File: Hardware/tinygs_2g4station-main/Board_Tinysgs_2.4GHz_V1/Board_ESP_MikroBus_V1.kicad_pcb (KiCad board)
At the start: 2 copper layers, 103.6 x 61.7 mm, 26 parts, among them U1 ESP32-DEVKITC-32D

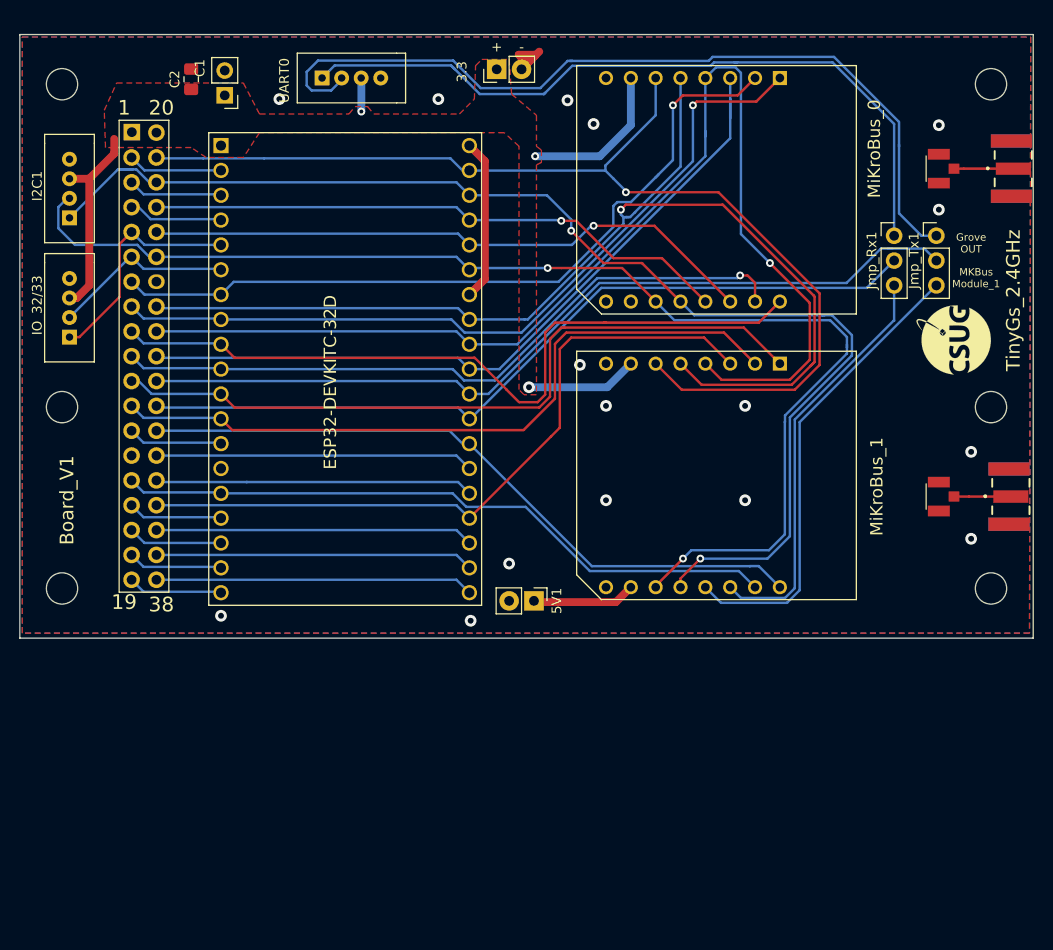
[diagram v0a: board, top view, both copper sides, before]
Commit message: Here is a version with the ISA connector standard. The schematic is ready, but the layout needs to be fixed
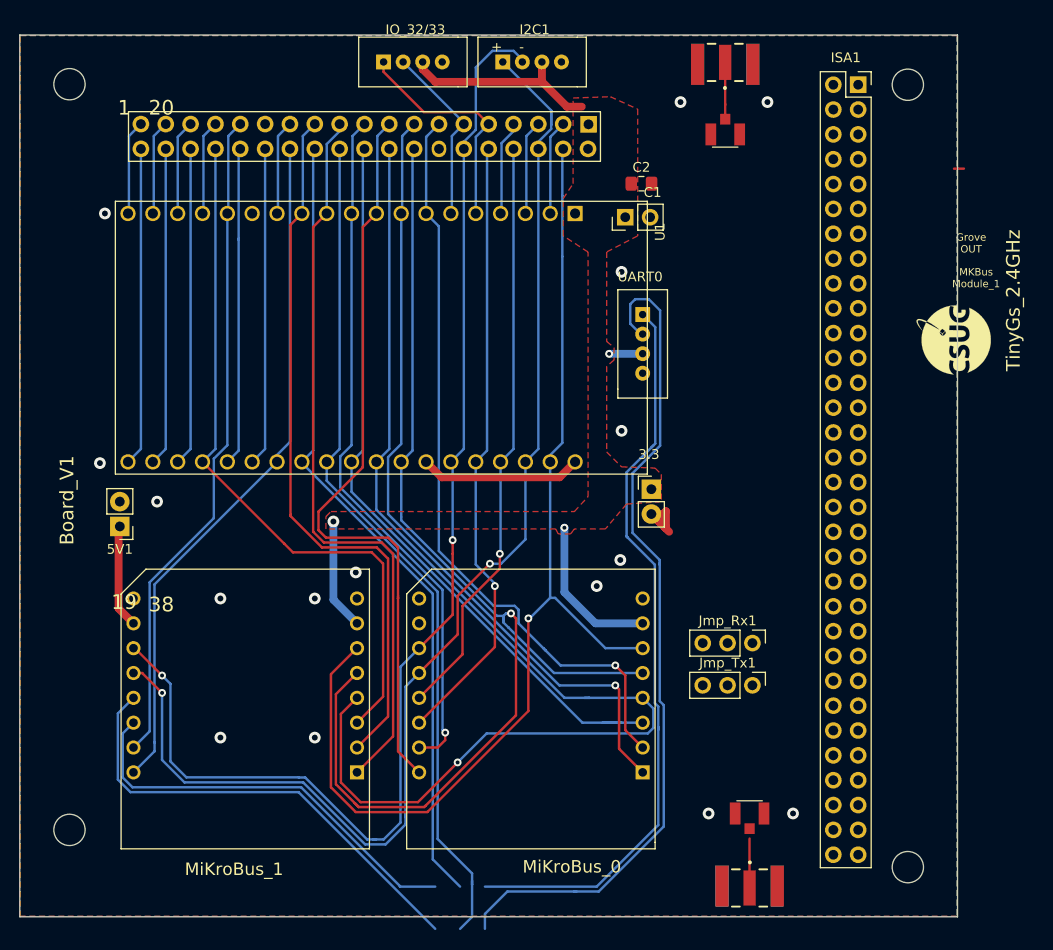
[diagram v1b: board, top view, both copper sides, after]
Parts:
- removed the REF** at (48.0, 55.1)
- removed the REF** at (143.0, 55.1)
- added ISA1: Conn_02x32_Odd_Even, Connector_PinSocket_2.54mm:PinSocket_2x32_P2.54mm_Vertical, F.Cu at (129.4, 22.1)
- U1: footprint ESP32-DEVKITC-32D:MODULE_ESP32-DEVKITC-V4-32D -> ESP32-DEVKITC-32D:MODULE_ESP32-DEVKITC-32D
- moved SMA_2 78.3 mm to (118.3, 104.3), turned to 0 degrees
- moved MiKroBus_0 72.4 mm to (107.4, 92.5), turned to 180 degrees
- moved UFL_2 68.7 mm to (118.3, 96.7), turned to 0 degrees
- moved MiKroBus_1 60.1 mm to (78.2, 92.5), turned to 180 degrees
- moved SMA_1 53.1 mm to (115.8, 19.9), turned to 180 degrees
- moved I2C1 52.2 mm to (96.1, 17.3), turned to 0 degrees
- moved Connector_2x19 51.8 mm to (104.3, 23.6), turned to -90 degrees
- moved Jmp_Tx1 49.7 mm to (118.6, 83.6), turned to -90 degrees
- moved C2 47.3 mm to (107.3, 32.3), turned to 0 degrees
- moved IO_32/33 46.7 mm to (83.9, 17.3), turned to 0 degrees
- moved 3.3 45.8 mm to (108.3, 63.5), turned to 0 degrees
- moved Jmp_Rx1 44.1 mm to (118.6, 79.2), turned to -90 degrees
- moved UART0 43.9 mm to (109.9, 48.7), turned to -90 degrees
- moved 5V1 43.0 mm to (53.9, 67.3), turned to 180 degrees
- moved UFL_1 43.0 mm to (115.8, 27.2), turned to 180 degrees
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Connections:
- MiKroBus_0 pad 15: Net-(MiKroBus_0-Pad15) -> unconnected-(MiKroBus_0-Pad15)
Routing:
- net Net-(SMA_2-Pad1): track 6.07 -> 5.05 mm
- net /16: track 9.90 -> 10.9 mm
- net GNDREF: vias 16 -> 15
- net +3V3: vias 3 -> 4
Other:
- board size 103.6 x 61.7 mm -> 95.9 x 90.2 mm
- net class Default removed
- net class Power removed
- net class data removed

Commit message: Uart groove repositioned
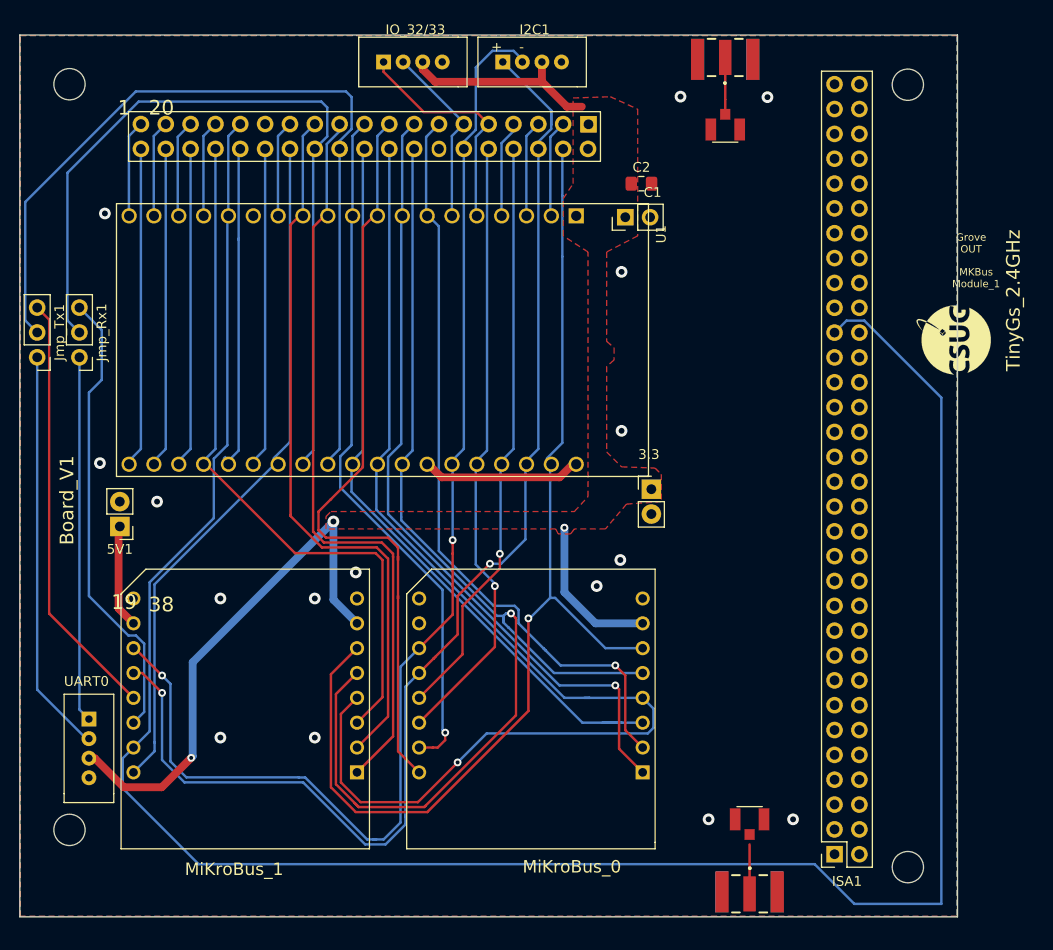
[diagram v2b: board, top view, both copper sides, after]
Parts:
- moved Jmp_Tx1 80.5 mm to (45.5, 50.0), turned to 180 degrees
- moved ISA1 78.7 mm to (127.0, 100.8), turned to 180 degrees
- moved Jmp_Rx1 74.8 mm to (49.8, 50.0), turned to 180 degrees
- moved UART0 70.1 mm to (53.3, 90.0)
- moved UFL_2 0.60 mm to (118.3, 97.3)
- moved SMA_2 0.60 mm to (118.3, 104.9)
- moved SMA_1 0.50 mm to (115.8, 19.4)
- moved UFL_1 0.50 mm to (115.8, 26.7)
- moved U1 0.27 mm to (80.8, 48.3)
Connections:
- ISA1 pad 1: (no net) -> unconnected-(ISA1-Pad1)
- ISA1 pad 10: (no net) -> unconnected-(ISA1-Pad10)
- ISA1 pad 12: (no net) -> unconnected-(ISA1-Pad12)
- ISA1 pad 14: (no net) -> unconnected-(ISA1-Pad14)
- ISA1 pad 16: (no net) -> unconnected-(ISA1-Pad16)
- ISA1 pad 18: (no net) -> unconnected-(ISA1-Pad18)
- ISA1 pad 2: (no net) -> GND
- ISA1 pad 20: (no net) -> GND
- ISA1 pad 22: (no net) -> unconnected-(ISA1-Pad22)
- ISA1 pad 24: (no net) -> unconnected-(ISA1-Pad24)
- ISA1 pad 26: (no net) -> unconnected-(ISA1-Pad26)
- ISA1 pad 28: (no net) -> unconnected-(ISA1-Pad28)
- ISA1 pad 30: (no net) -> unconnected-(ISA1-Pad30)
- ISA1 pad 32: (no net) -> unconnected-(ISA1-Pad32)
- ISA1 pad 34: (no net) -> unconnected-(ISA1-Pad34)
- ISA1 pad 36: (no net) -> unconnected-(ISA1-Pad36)
- ISA1 pad 38: (no net) -> unconnected-(ISA1-Pad38)
- ISA1 pad 4: (no net) -> unconnected-(ISA1-Pad4)
- ISA1 pad 40: (no net) -> unconnected-(ISA1-Pad40)
- ISA1 pad 42: (no net) -> unconnected-(ISA1-Pad42)
- ISA1 pad 44: (no net) -> unconnected-(ISA1-Pad44)
- ISA1 pad 45: (no net) -> unconnected-(ISA1-Pad45)
- ISA1 pad 46: (no net) -> unconnected-(ISA1-Pad46)
- ISA1 pad 47: (no net) -> unconnected-(ISA1-Pad47)
- ISA1 pad 48: (no net) -> unconnected-(ISA1-Pad48)
- ISA1 pad 49: (no net) -> unconnected-(ISA1-Pad49)
- ISA1 pad 50: (no net) -> unconnected-(ISA1-Pad50)
- ISA1 pad 51: (no net) -> unconnected-(ISA1-Pad51)
- ISA1 pad 52: (no net) -> unconnected-(ISA1-Pad52)
- ISA1 pad 53: (no net) -> unconnected-(ISA1-Pad53)
- ISA1 pad 54: (no net) -> unconnected-(ISA1-Pad54)
- ISA1 pad 55: (no net) -> unconnected-(ISA1-Pad55)
- ISA1 pad 56: (no net) -> unconnected-(ISA1-Pad56)
- ISA1 pad 57: (no net) -> unconnected-(ISA1-Pad57)
- ISA1 pad 59: (no net) -> unconnected-(ISA1-Pad59)
- ISA1 pad 60: (no net) -> unconnected-(ISA1-Pad60)
- ISA1 pad 61: (no net) -> unconnected-(ISA1-Pad61)
- ISA1 pad 62: (no net) -> GND
- ISA1 pad 63: (no net) -> GND
- ISA1 pad 64: (no net) -> GND
- ISA1 pad 8: (no net) -> unconnected-(ISA1-Pad8)
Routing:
- net INT_1: track 68.4 -> 228.1 mm
- net UART2_Tx_grove: track 86.7 -> 41.3 mm
- net +3V3: track 51.5 -> 91.1 mm, vias 4 -> 3
- net UART2_Rx_grove: track 76.4 -> 37.8 mm
- net GNDREF: track 24.3 -> 17.5 mm, vias 15 -> 16
- net UART2_Rx_MiKroBus: track 42.7 -> 47.2 mm
- net UART2_Tx_MiKroBus: track 47.8 -> 44.0 mm
- net UART2_Tx: track 87.3 -> 90.5 mm
- net UART2_Rx: track 82.9 -> 84.3 mm
- net /16: track 10.9 -> 9.90 mm

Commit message: The TinyGS in cubesat standard with ISA communication is done, all the wires are branched. Verification needed to ensure it's functionality and noise/EM immunity
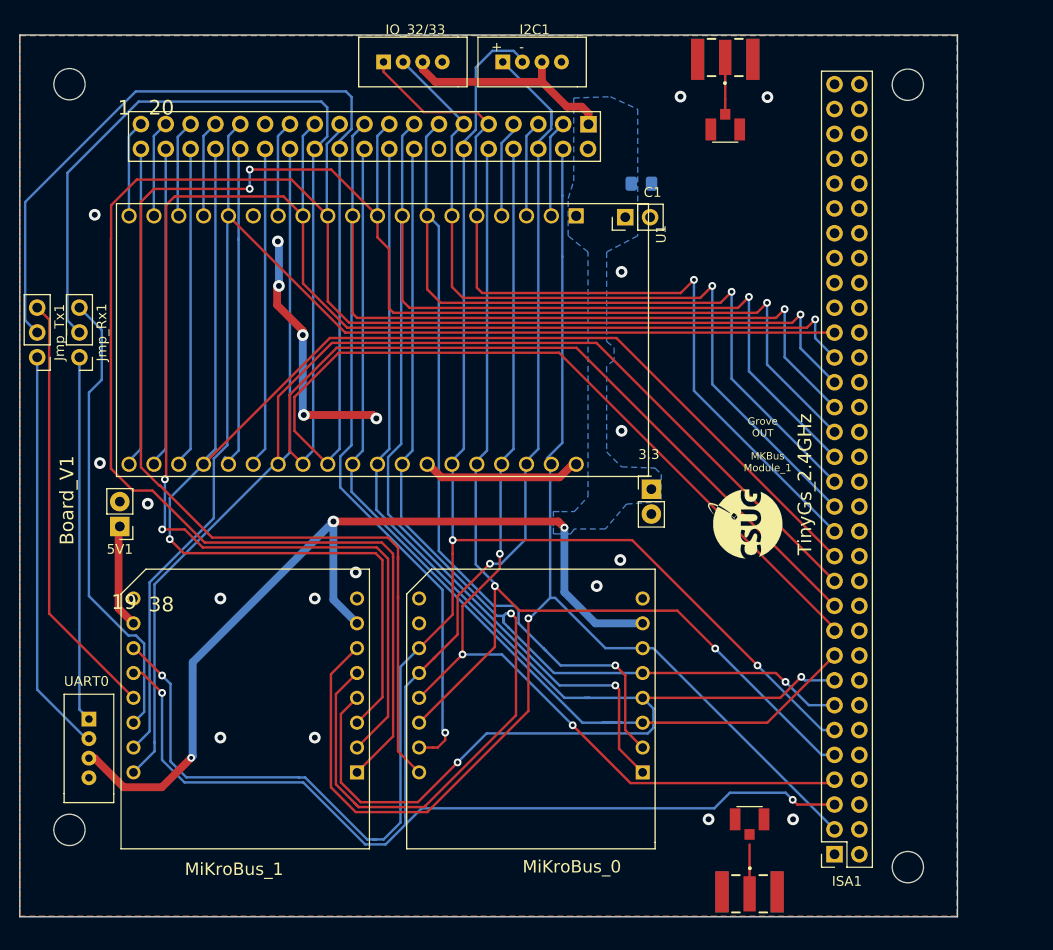
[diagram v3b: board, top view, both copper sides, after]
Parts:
- C2: moved to B.Cu
- moved G*** 28.4 mm to (117.9, 67.1)
- moved G*** 24.0 mm to (117.9, 37.1)
- moved G*** 17.1 mm to (117.0, 56.2)
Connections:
- ISA1 pad 58: +5V -> unconnected-(ISA1-Pad58)
- ISA1 pad 6: +5V -> unconnected-(ISA1-Pad6)
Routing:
- net AN_1: track 75.9 -> 184.6 mm, vias 0 -> 1
- net PWM_0: track 78.0 -> 185.1 mm, vias 0 -> 3
- net Reset_1: track 73.6 -> 169.5 mm, vias 0 -> 3
- net INT_1: track 228.1 -> 135.4 mm
- net NSS_1: track 72.7 -> 161.1 mm, vias 0 -> 1
- net UART2_Tx: track 90.5 -> 167.8 mm
- net PWM_1: track 70.2 -> 146.8 mm
- net UART2_Rx: track 84.3 -> 160.6 mm
- net INT_0: track 71.5 -> 138.4 mm, vias 1 -> 2
- net AN_0: track 81.6 -> 146.4 mm, vias 1 -> 2
- net Reset_0: track 78.6 -> 142.0 mm, vias 1 -> 2
- net IN35: track 18.7 -> 81.3 mm, vias 0 -> 1
- net IN34: track 23.8 -> 85.8 mm, vias 0 -> 1
- net I2C_SDA: track 128.0 -> 175.1 mm, vias 2 -> 3
- net I2C_SCL: track 128.8 -> 174.8 mm, vias 2 -> 3
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- added copper zone on B.Cu, net +3V3
- removed copper zone on F.Cu, net +3V3
